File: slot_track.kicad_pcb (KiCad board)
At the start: 4 copper layers, 212.5 x 152.6 mm, 39 parts, among them J1 Barrel_Jack_Switch, J2 SWD Debug, T1 LinearTouch4, T2 Conn_01x01, T3 LinearTouch4, U1 STM32F051C6Tx, U2 MCP1754S-3302xCB, U3 ZXBM5210-SP, U4 ZXBM5210-SP, U5 ZXBM5210-SP

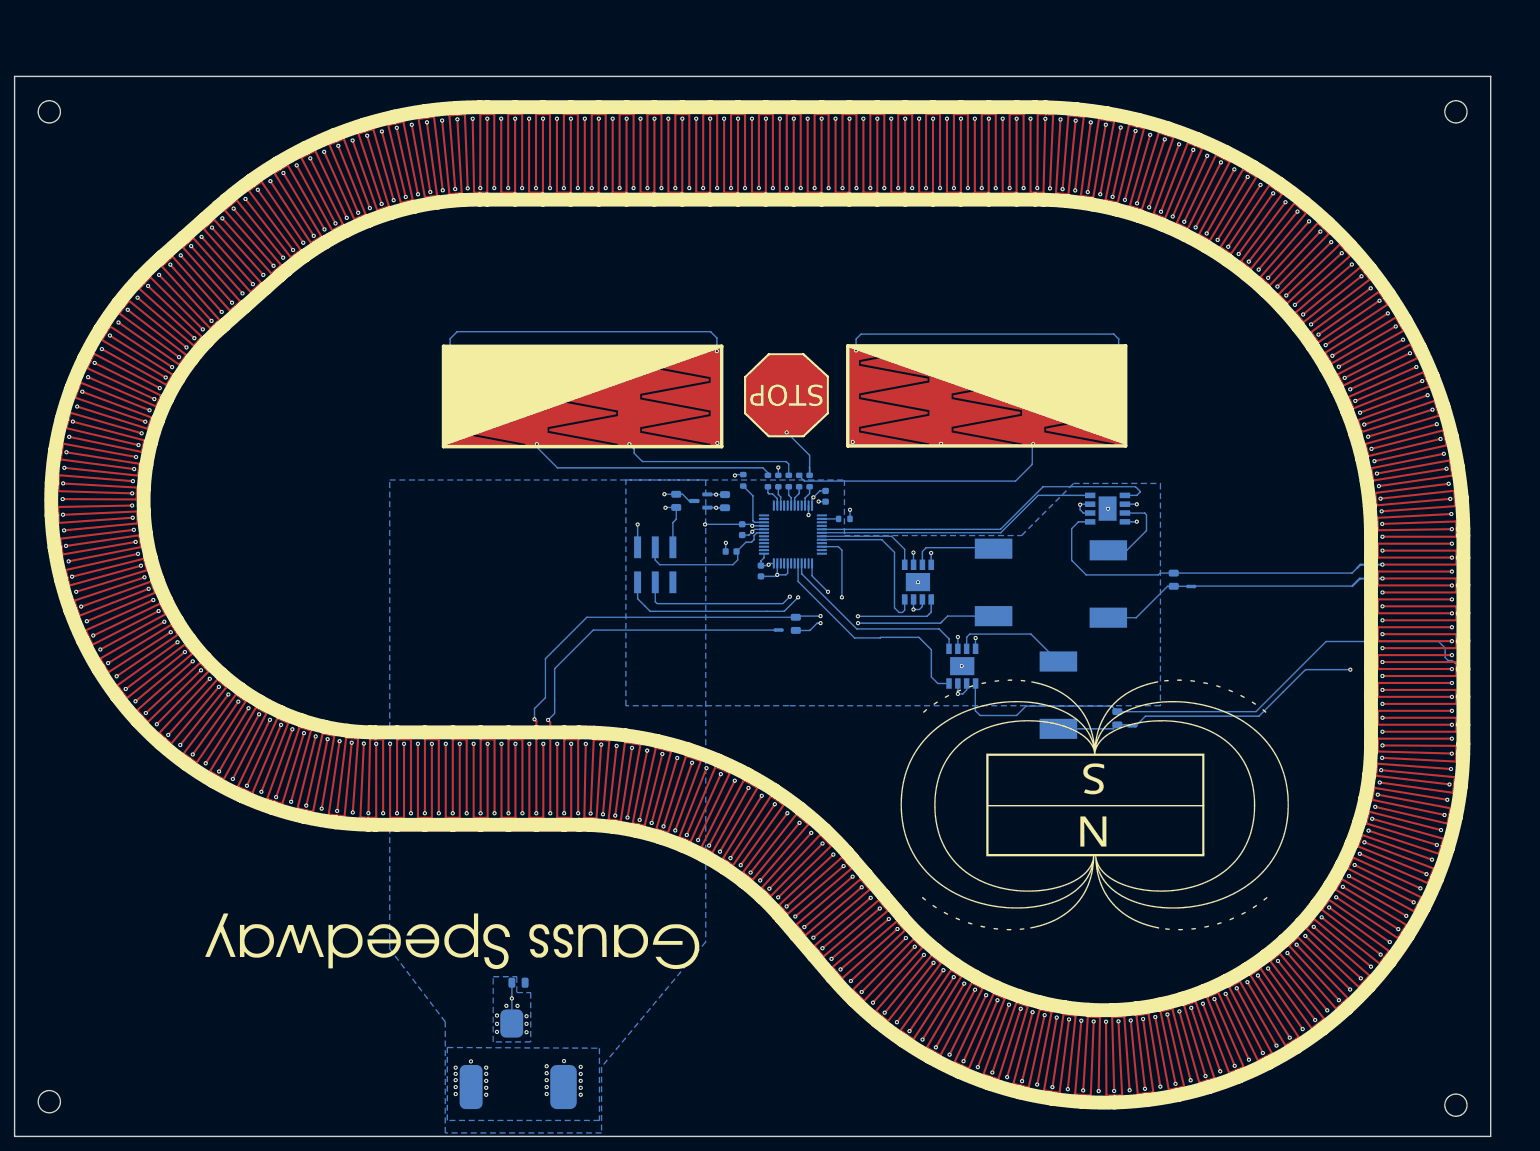
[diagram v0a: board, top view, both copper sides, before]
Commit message: Rev 2
- Adjusts track shape
- Swaps guard rails to top and phase to In1. Hopefully this lowers the
noise and friction.
- Adds sample caps
- Adds SWCLK resistor
- Adds divider for Vin measurement
- Switches to a PH connector for SWD and a UART
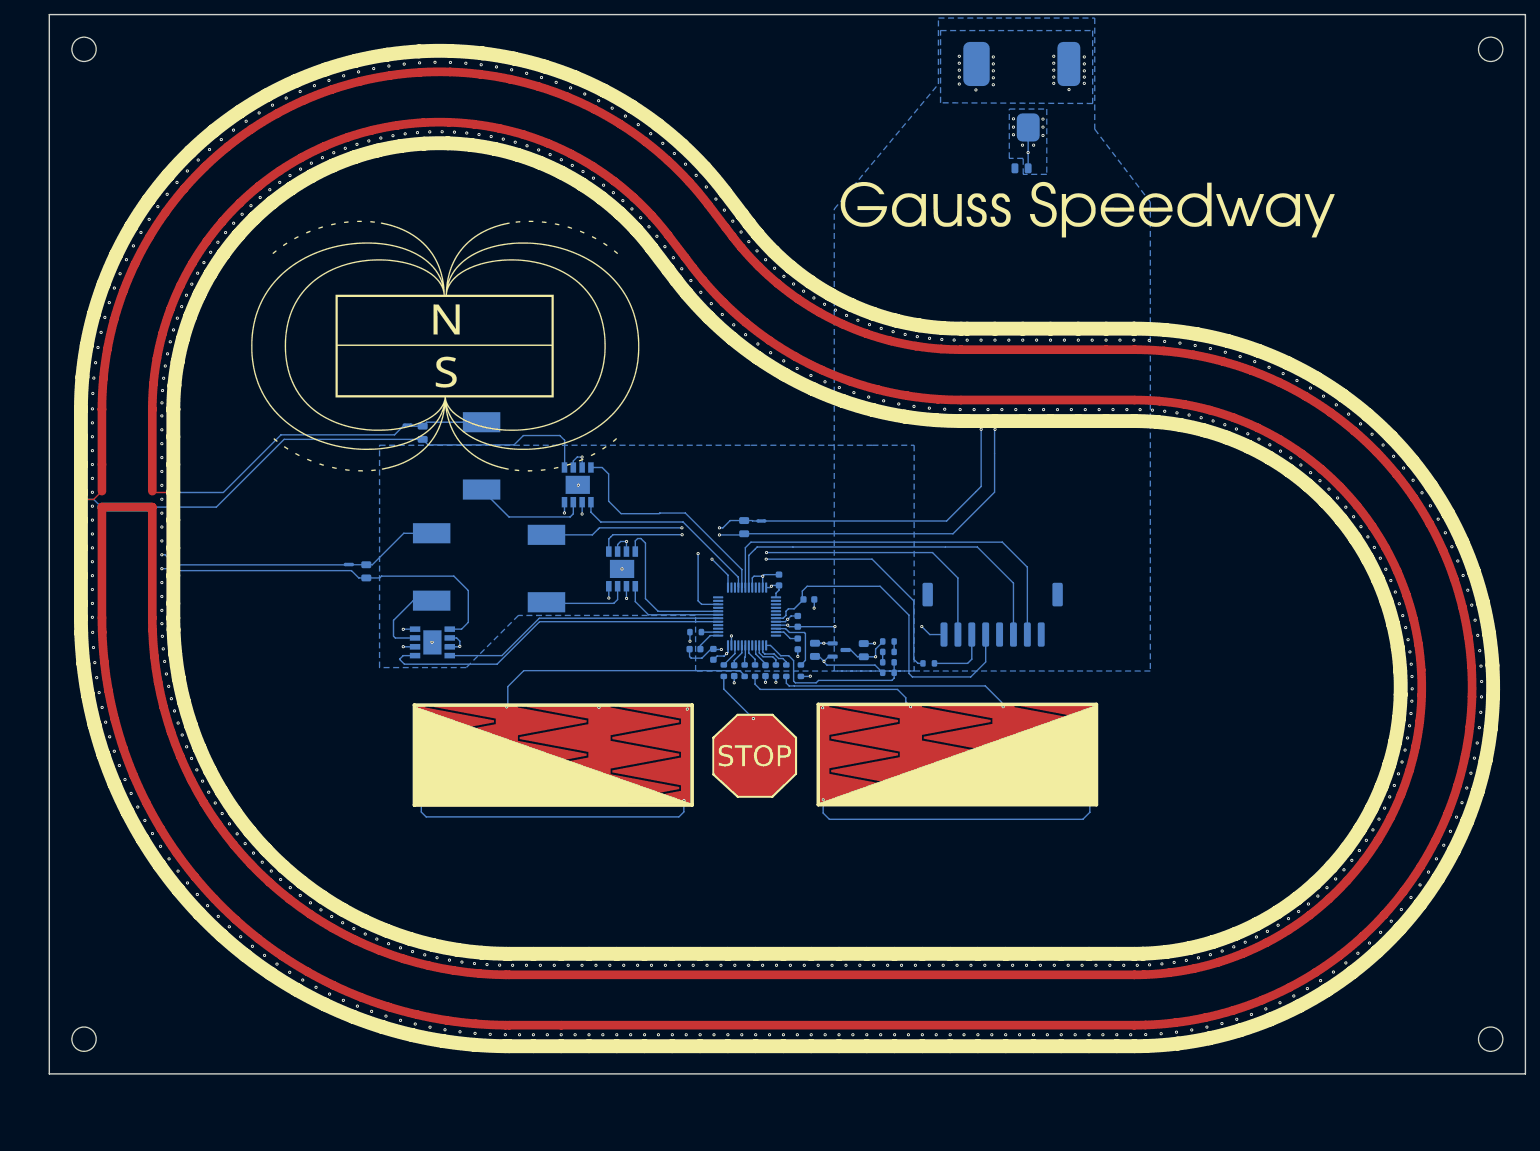
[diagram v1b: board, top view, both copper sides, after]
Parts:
- added C11: 47nF, Capacitor_SMD:C_0603_1608Metric, B.Cu at (200.2, 147.6)
- added C12: 47nF, Capacitor_SMD:C_0603_1608Metric, B.Cu at (195.6, 151.4)
- added C13: 47nF, Capacitor_SMD:C_0603_1608Metric, B.Cu at (191.1, 151.4)
- added C14: 47nF, Capacitor_SMD:C_0603_1608Metric, B.Cu at (185.4, 148.3)
- added R10: 1k, Resistor_SMD:R_0603_1608Metric, B.Cu at (213.3, 150.2)
- added R11: 1k, Resistor_SMD:R_0603_1608Metric, B.Cu at (213.3, 151.8)
- added R12: 1k, Resistor_SMD:R_0603_1608Metric, B.Cu at (219.1, 150.4)
- added R8: 1k, Resistor_SMD:R_0603_1608Metric, B.Cu at (213.3, 147.2)
- added R9: 1k, Resistor_SMD:R_0603_1608Metric, B.Cu at (213.3, 148.8)
- G1: renamed from Ref**; value Val** -> Graphic; footprint track_project:magnetlogo -> track:magnetlogo
- H1, H2, H3, H4: footprint MountingHole:MountingHole_3.2mm_M3 -> MountingHole:MountingHole_3.5mm
- J2: value SWD Debug -> JST PH; footprint Connector_PinHeader_2.54mm:PinHeader_2x03_P2.54mm_Vertical_SMD -> Connector_JST:JST_PH_S8B-PH-SM4-TB_1x08-1MP_P2.00mm_Horizontal
- moved H3 256.9 mm to (300.0, 62.0), turned to 180 degrees
- moved H1 249.2 mm to (97.5, 62.0), turned to 180 degrees
- moved H2 246.7 mm to (300.0, 204.5), turned to 180 degrees
- moved H4 238.4 mm to (97.5, 204.5), turned to 180 degrees
- moved J1 176.5 mm to (232.6, 57.4), turned to 0 degrees
- moved G*** 139.5 mm to (242.0, 85.1), turned to 0 degrees
- moved C3 137.8 mm to (232.5, 79.1), turned to 180 degrees
- moved G1 129.3 mm to (136.5, 113.0), turned to 0 degrees
- moved NT2 121.3 mm to (135.6, 136.2), turned to 180 degrees
- moved C10 116.2 mm to (138.1, 137.2), turned to 90 degrees
- moved NT5 112.9 mm to (144.1, 116.1), turned to 180 degrees
- moved C9 108.1 mm to (146.2, 117.2), turned to 90 degrees
- moved T3 107.1 mm to (243.2, 163.5), turned to 180 degrees
- moved U3 99.1 mm to (147.7, 147.4), turned to 180 degrees
- moved L2 97.4 mm to (147.5, 136.5), turned to 90 degrees
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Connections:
- J2 pad 3: /NRST -> /SWCLK
- J2 pad 4: /SWCLK -> /NRST
- J2 pad 5: GND -> unconnected-(J2-Pad5)
- J2 pad 6: unconnected-(J2-Pad6) -> /UART_RX
- U1 pad 11: unconnected-(U1-Pad11) -> /G1_SAMPLE
- U1 pad 13: unconnected-(U1-Pad13) -> /VBUS_SENSE
- U1 pad 16: unconnected-(U1-Pad16) -> /G2_SAMPLE
- U1 pad 20: unconnected-(U1-Pad20) -> /G3_SAMPLE
- U1 pad 25: unconnected-(U1-Pad25) -> /G6_SAMPLE
- U1 pad 37: /SWCLK -> Net-(U1-Pad37)
- U1 pad 42: unconnected-(U1-Pad42) -> /UART_TX
- U1 pad 43: unconnected-(U1-Pad43) -> /UART_RX
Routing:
- net /UART_TX: track 0.00 -> 57.9 mm
- net /UART_RX: track 0.00 -> 52.8 mm
- net Net-(U1-Pad37): track 0.00 -> 46.5 mm, vias 0 -> 2
- net /NRST: track 21.0 -> 48.6 mm
- net GND: track 29.4 -> 55.9 mm, vias 35 -> 38
- net /VBUS_SENSE: track 0.00 -> 24.9 mm
- net /SWCLK: track 33.5 -> 9.17 mm, vias 2 -> 0
- net /1B_P: track 3422.1 -> 3445.4 mm, vias 264 -> 266
- net /1A_P: track 3453.9 -> 3476.4 mm, vias 268 -> 270
- net /SWDIO: track 43.2 -> 57.0 mm
- net /G1_P: track 1182.7 -> 1189.0 mm
- net /STOP: track 8.74 -> 13.3 mm
- net /G6_SAMPLE: track 0.00 -> 3.68 mm
- net /G1_SAMPLE: track 0.00 -> 3.52 mm
- net /G2_SAMPLE: track 0.00 -> 3.44 mm
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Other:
- board size 212.5 x 152.6 mm -> 212.5 x 152.5 mm
- board text added: "GND"
- board text added: "Gauss Speedway Rev 2"
- board text added: "RX"
- board text added: "SWCLK"
- board text added: "SWDIO"
- board text added: "TX"
- board text added: "VCC"
- board text added: "nRST"
